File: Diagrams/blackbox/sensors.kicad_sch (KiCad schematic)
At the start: 2 parts, among them U8 RAZOR 9dof IMU, U9 BNO055

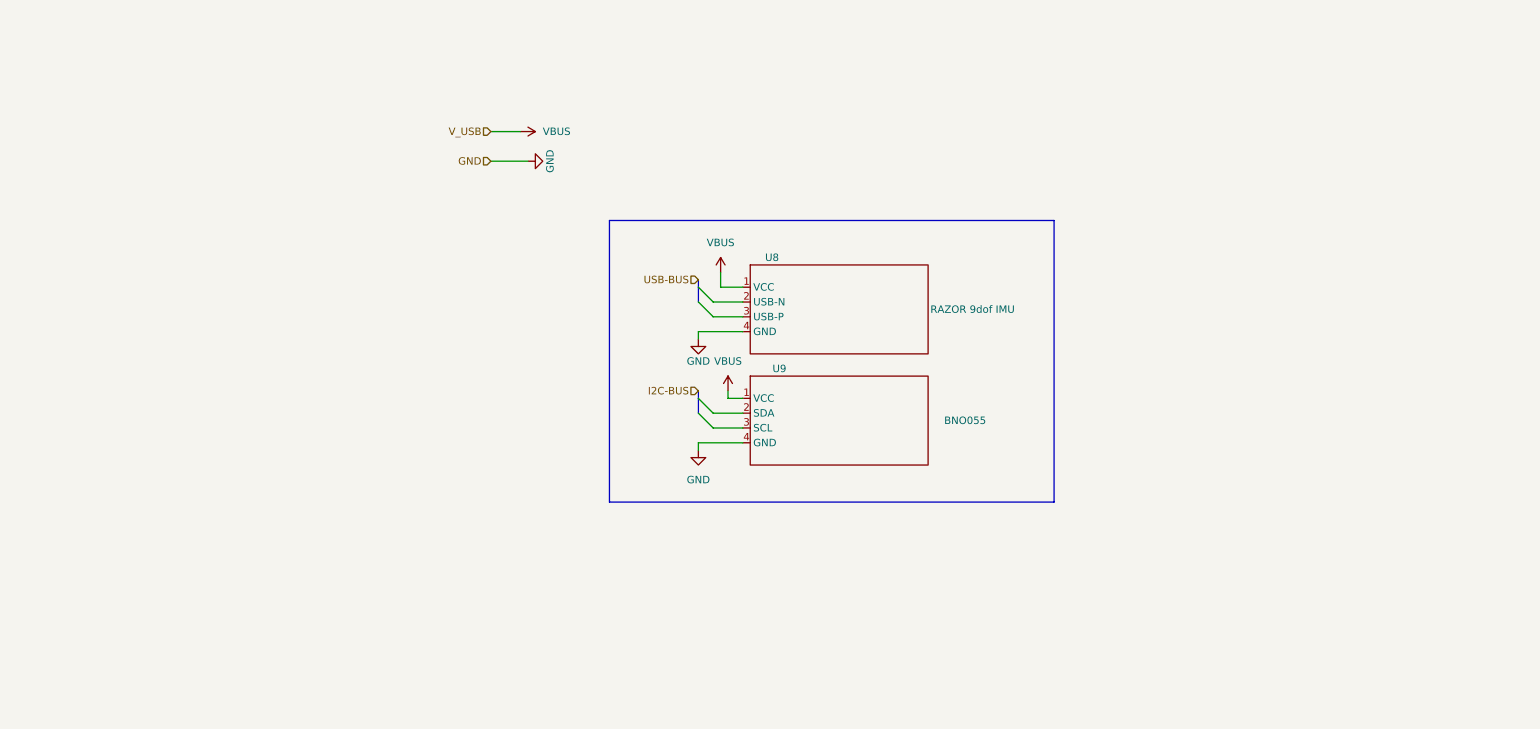
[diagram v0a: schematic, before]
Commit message: Blackbox Diagram V1 Completed
Top to Down Blok Şeması Oluşturulmuştur. Oluşturulan Hiyerarşik Yapının PDF Çıktısı Oluşturulmuştur.
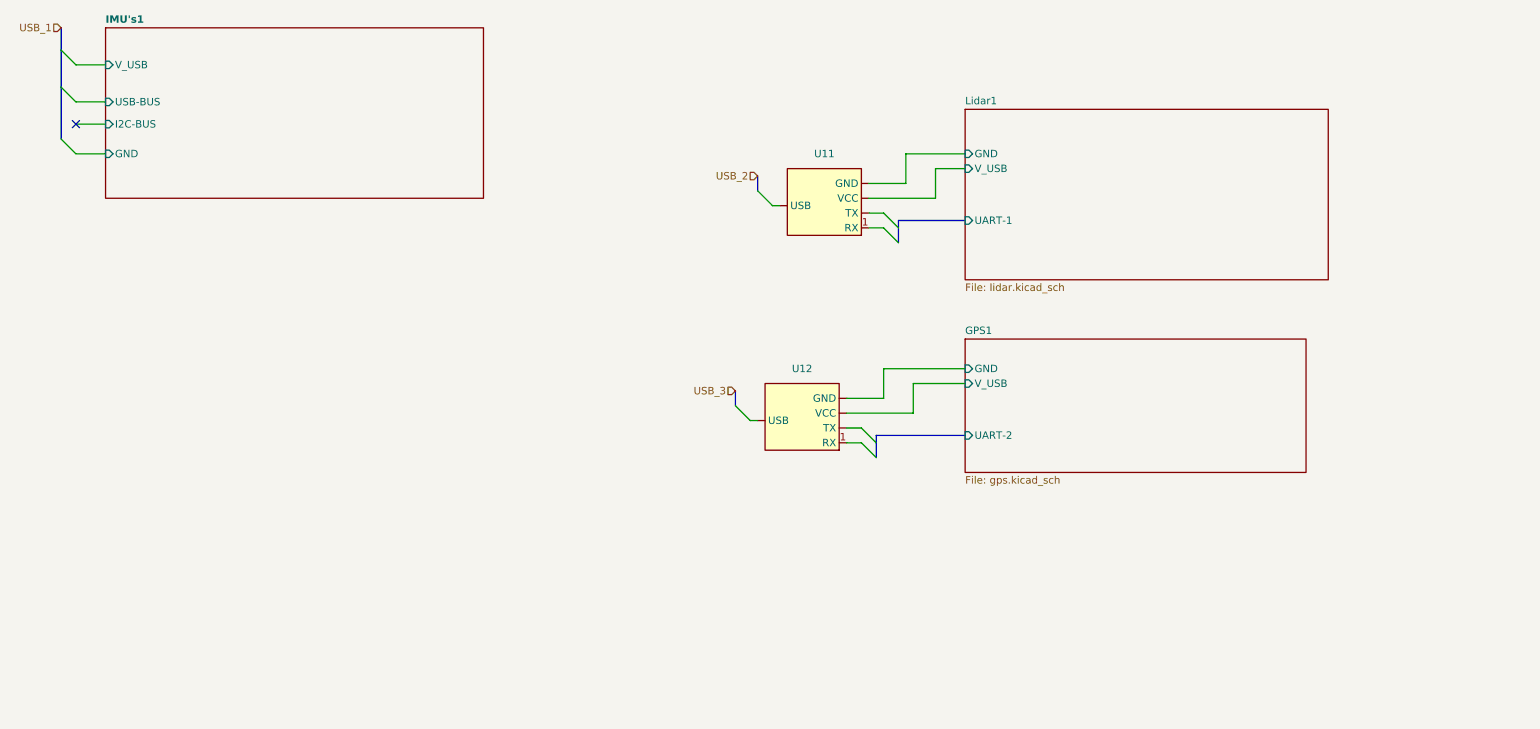
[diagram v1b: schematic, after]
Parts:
- removed U8: RAZOR 9dof IMU, symbol bitirme:Sparkfun_IMU_Razor
- removed U9: BNO055, symbol bitirme:Sparkfun_IMU_Razor
- added U11, U12: ~, symbol bitirme:USBtoTTL
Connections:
- new net GPS1/GND: U12. (VCC)
- new net GPS1/V_USB: U12. (VCC)
- new net Lidar1/GND: U11. (VCC)
- new net Lidar1/V_USB: U11. (VCC)
- no-connect marks 0 -> 1
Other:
- added sheet GPS1 (gps.kicad_sch)
- added sheet IMU's1 (Microcontroller.kicad_sch)
- added sheet Lidar1 (lidar.kicad_sch)

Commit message: Blackbox Diagram V1.1
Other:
- note added: "GPS"
- note added: "IMU"
- note added: "LIDAR"
